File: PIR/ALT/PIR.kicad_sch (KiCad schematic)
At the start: 29 parts, among them J1 BUS, J2 BATT_EXT, J5 FLASH/CONF, J6 PIR, Q1 BC846, Q2 BC846, Q3 BC857, SW1 tamper switch, U1 AP63203WU, U2 WT8266-S1

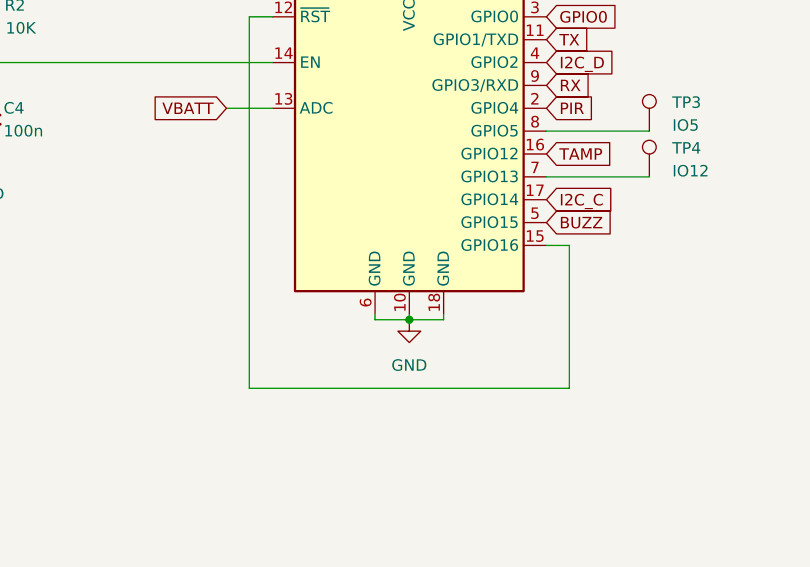
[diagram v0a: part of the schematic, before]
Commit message: Update symbol and footprint of WT8266
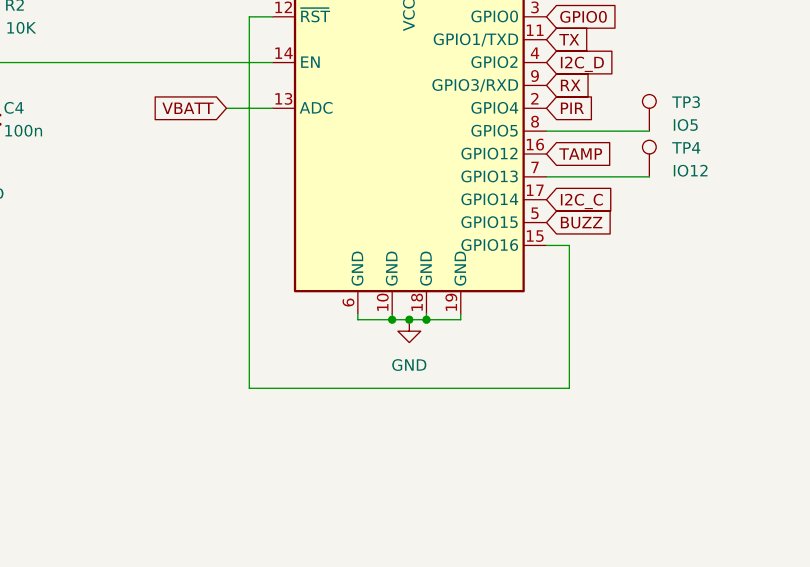
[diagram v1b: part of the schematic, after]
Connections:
- net GND: now also U2.19 (GND)

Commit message: Fix incident
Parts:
- added R6: 10k, Resistor_SMD:R_0603_1608Metric, symbol Device:R
- renumbered J6 to J3, J5 to J4, R6 to R7, TP6 to TP2
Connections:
- net +3.3V: now also R6.1
- net GPIO0: now also R6.2
- net at C2.2, L1.1: now also U1.5 (SW); no longer U1.6 (BST)
- net at C2.1: now also U1.6 (BST); no longer U1.5 (SW)
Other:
- moved on the sheet: C2, C3, C5, L1, TP2
